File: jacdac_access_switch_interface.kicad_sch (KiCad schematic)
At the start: 43 parts

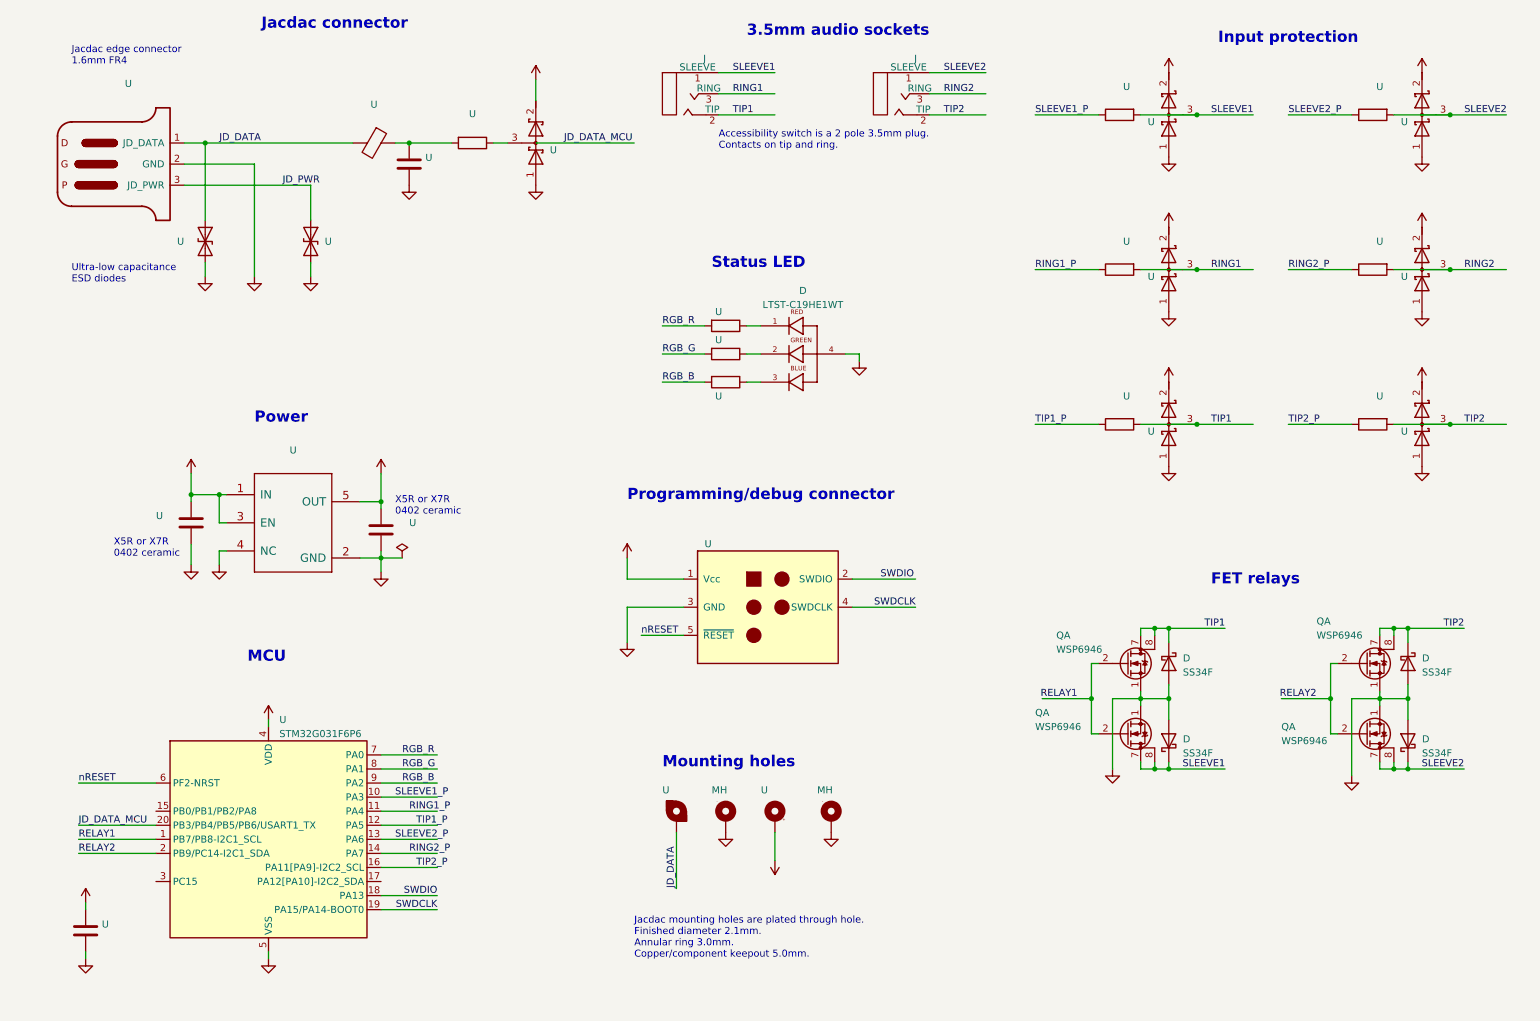
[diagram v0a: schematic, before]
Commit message: Changed MCU to STM32G030F6P6, updated input protection resistor to 10K, updated audio symbol
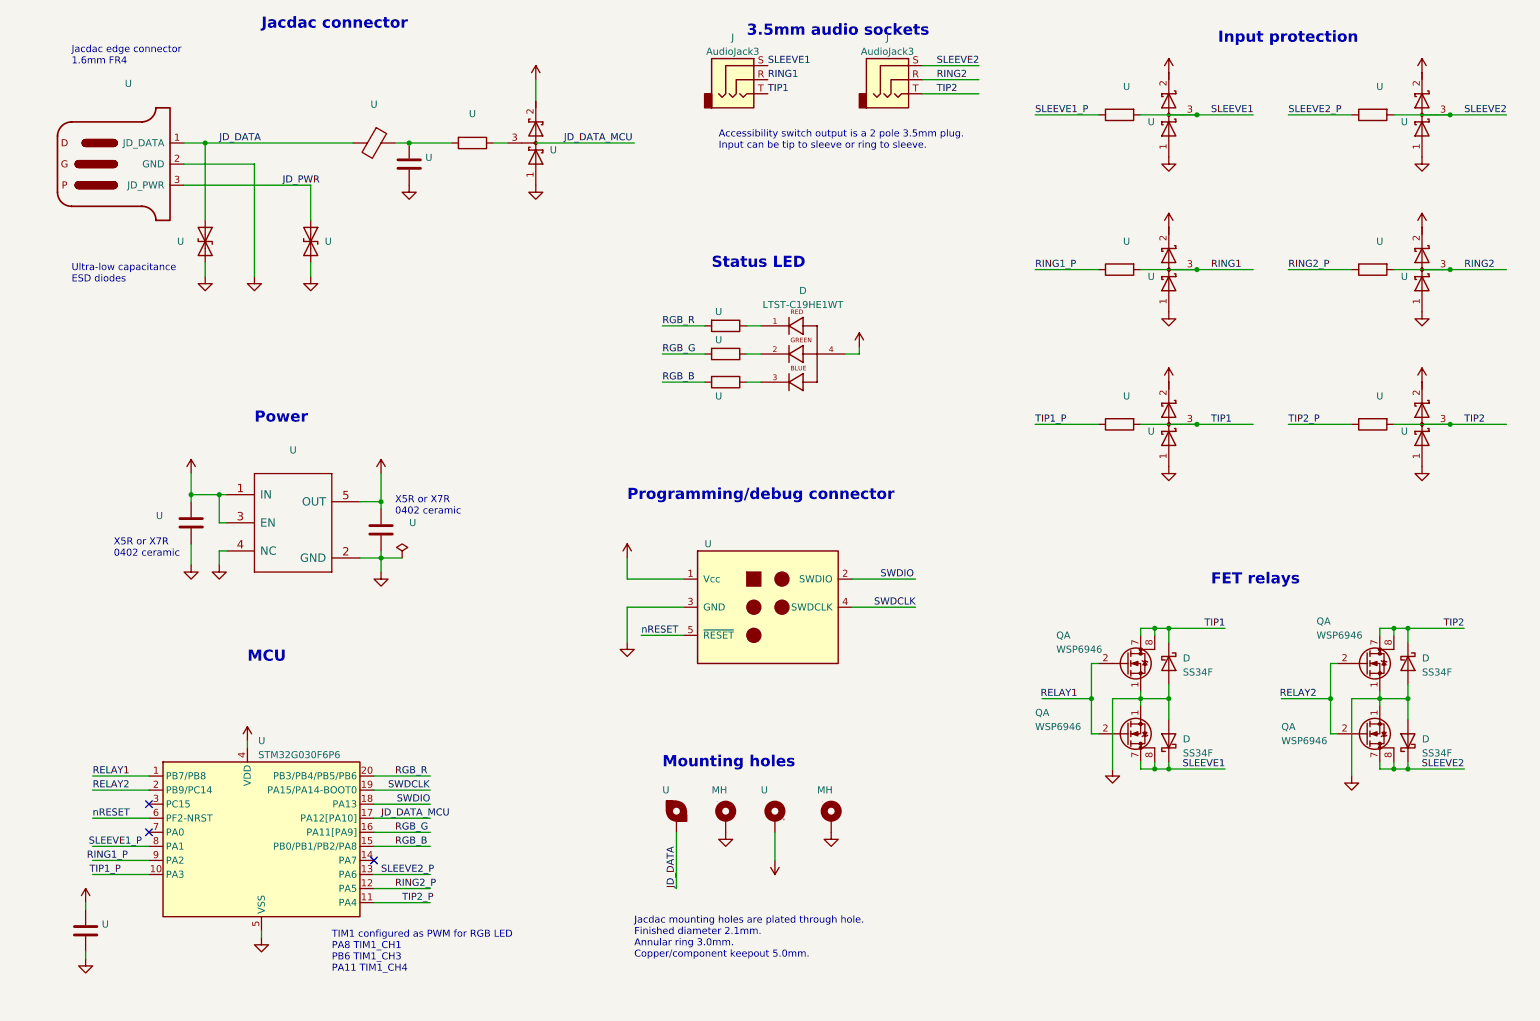
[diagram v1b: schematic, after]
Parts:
- removed J (x2): jack_3.5_pj313d, jacdac_access_switch_interface:jack_3.5_pj313d_smt, symbol jacdac_access_switch_interface:jack_3.5_pj313d
- removed U: STM32G031F6P6, Package_SO:TSSOP-20_4.4x6.5mm_P0.65mm, symbol jacdac_access_switch_interface:STM32G031F6P6
- added J (x2): AudioJack3, symbol jacdac_access_switch_interface:AudioJack3
- added U: STM32G030F6P6, jacdac_access_switch_interface:TSSOP-20_4.4x6.5mm_P0.65mm, symbol jacdac_access_switch_interface:STM32G030F6P6
- U: LCSC C138065 -> C60490
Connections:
- net +3V3: now also D.4, U.4 (VDD)
- net GND: now also U.5 (VSS); no longer D.4
- net JD_DATA_MCU: now also U.17 (PA12[PA10])
- net RELAY1: now also U.1 (PB7/PB8)
- net RELAY2: now also U.2 (PB9/PC14)
- net RGB_B: now also U.15 (PB0/PB1/PB2/PA8)
- net RGB_G: now also U.16 (PA11[PA9])
- net RGB_R: now also U.20 (PB3/PB4/PB5/PB6)
- net RING1: now also J.R
- net RING1_P: now also U.9 (PA2)
- net RING2: now also J.R
- net RING2_P: now also U.12 (PA5)
- net SLEEVE1: now also J.S
- net SLEEVE1_P: now also U.8 (PA1)
- net SLEEVE2: now also J.S
- net SLEEVE2_P: now also U.13 (PA6)
- net SWDCLK: now also U.19 (PA15/PA14-BOOT0)
- net SWDIO: now also U.18 (PA13)
- net TIP1: now also J.T
- net TIP1_P: now also U.10 (PA3)
- net TIP2: now also J.T
- net TIP2_P: now also U.11 (PA4)
- net nRESET: now also U.6 (PF2-NRST)
- no-connect marks 0 -> 3
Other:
- note added: "Accessibility switch output is a 2 pole 3.5mm plug. Input can be tip to sleeve or ring to sleeve."
- note added: "TIM1 configured as PWM for RGB LED PA8 TIM1_CH1 PB6 TIM1_CH3 PA11 TIM1_CH4"
- note removed: "Accessibility switch is a 2 pole 3.5mm plug. Contacts on tip and ring."

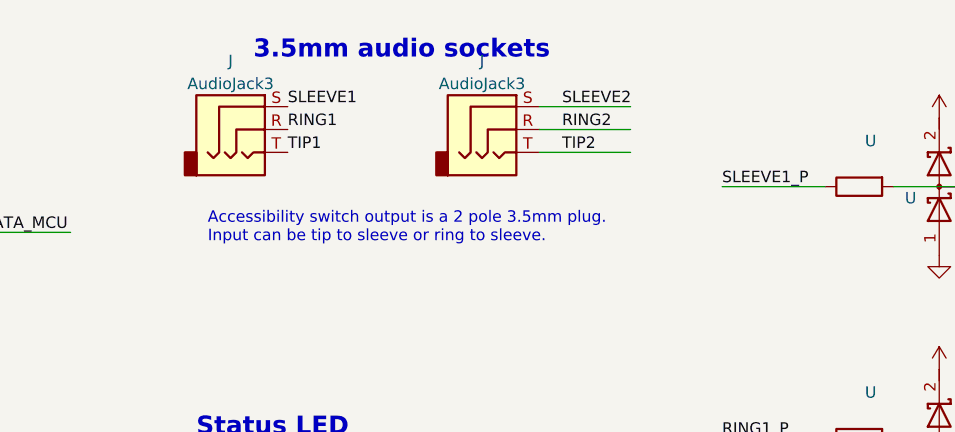
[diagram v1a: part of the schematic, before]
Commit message: Updated audio socket symbol
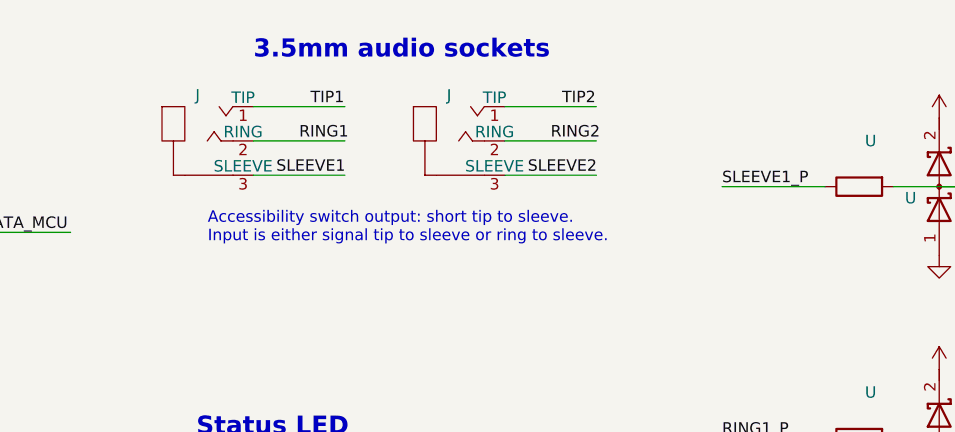
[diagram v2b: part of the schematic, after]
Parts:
- removed J (x2): AudioJack3, symbol jacdac_access_switch_interface:AudioJack3
- added J (x2): 54-00036_audio_plug, jacdac_access_switch_interface:Tensility-54-00036-0, symbol jacdac_access_switch_interface:54-00036_audio_plug
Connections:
- net RING1: now also J.2 (RING)
- net RING2: now also J.2 (RING)
- net SLEEVE1: now also J.3 (SLEEVE)
- net SLEEVE2: now also J.3 (SLEEVE)
- net TIP1: now also J.1 (TIP)
- net TIP2: now also J.1 (TIP)
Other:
- note added: "Accessibility switch output: short tip to sleeve. Input is either signal tip to sleeve or ring to sleeve."
- note removed: "Accessibility switch output is a 2 pole 3.5mm plug. Input can be tip to sleeve or ring to sleeve."
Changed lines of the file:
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@@
     (stroke (width 0) (type default))
   )
-  (wire (pts (xy 173.99 26.67) (xy 184.15 26.67))
+  (wire (pts (xy 170.18 34.29) (xy 180.34 34.29))
     (stroke (width 0) (type default))
   )
@@
     (stroke (width 0) (type default))
   )
+  (wire (pts (xy 142.24 34.29) (xy 152.4 34.29))
+    (stroke (width 0) (type default))
+  )
   (wire (pts (xy 76.2 105.41) (xy 76.2 106.68))
     (stroke (width 0) (type default))
@@
     (stroke (width 0) (type default))
   )
-  (wire (pts (xy 173.99 29.21) (xy 184.15 29.21))
-    (stroke (width 0) (type default))
-  )
-  (wire (pts (xy 173.99 31.75) (xy 184.15 31.75))
+  (wire (pts (xy 170.18 30.48) (xy 180.34 30.48))
+    (stroke (width 0) (type default))
+  )
+  (wire (pts (xy 170.18 26.67) (xy 180.34 26.67))
     (stroke (width 0) (type default))
   )
@@
     (stroke (width 0) (type default))
   )
+  (wire (pts (xy 142.24 26.67) (xy 152.4 26.67))
+    (stroke (width 0) (type default))
+  )
   (wire (pts (xy 256.54 153.67) (xy 259.08 153.67))
     (stroke (width 0) (type default))
@@
   )
   (wire (pts (xy 259.08 35.56) (xy 269.24 35.56))
+    (stroke (width 0) (type default))
+  )
+  (wire (pts (xy 142.24 30.48) (xy 152.4 30.48))
     (stroke (width 0) (type default))
   )
@@
     (effects (font (size 2.0066 2.0066) (thickness 0.4013) bold) (justify left bottom))
   )
-  (text "Accessibility switch output is a 2 pole 3.5mm plug. \nInput can be tip to sleeve or ring to sleeve."
+  (text "Accessibility switch output: short tip to sleeve.\nInput is either signal tip to sleeve or ring to sleeve."
     (at 137.16 41.91 0)
     (effects (font (size 1.27 1.27)) (justify left bottom))
@@
     (effects (font (size 1.27 1.27)) (justify left bottom))
   )
+  (label "RING1" (at 147.32 30.48 0) (fields_autoplaced)
+    (effects (font (size 1.27 1.27)) (justify left bottom))
+  )
   (label "RELAY1" (at 24.13 154.94 0) (fields_autoplaced)
     (effects (font (size 1.27 1.27)) (justify left bottom))
   )
-  (label "TIP2" (at 176.53 31.75 0) (fields_autoplaced)
+  (label "TIP2" (at 176.53 26.67 0) (fields_autoplaced)
     (effects (font (size 1.27 1.27)) (justify left bottom))
   )
@@
     (effects (font (size 1.27 1.27)) (justify right bottom))
   )
-  (label "TIP1" (at 146.05 31.75 0) (fields_autoplaced)
-    (effects (font (size 1.27 1.27)) (justify left bottom))
-  )
-  (label "RING2" (at 176.53 29.21 0) (fields_autoplaced)
+  (label "RING2" (at 175.26 30.48 0) (fields_autoplaced)
     (effects (font (size 1.27 1.27)) (justify left bottom))
   )
@@
     (effects (font (size 1.27 1.27)) (justify right bottom))
   )
+  (label "TIP1" (at 148.59 26.67 0) (fields_autoplaced)
+    (effects (font (size 1.27 1.27)) (justify left bottom))
+  )
   (label "SLEEVE2" (at 271.78 35.56 0) (fields_autoplaced)
     (effects (font (size 1.27 1.27)) (justify left bottom))
   )
-  (label "RING1" (at 146.05 29.21 0) (fields_autoplaced)
-    (effects (font (size 1.27 1.27)) (justify left bottom))
-  )
   (label "JD_DATA_MCU" (at 109.22 40.64 0) (fields_autoplaced)
     (effects (font (size 1.27 1.27)) (justify left bottom))
@@
   )
   (label "JD_DATA" (at 46.99 40.64 0) (fields_autoplaced)
-    (effects (font (size 1.27 1.27)) (justify left bottom))
-  )
-  (label "SLEEVE1" (at 146.05 26.67 0) (fields_autoplaced)
     (effects (font (size 1.27 1.27)) (justify left bottom))
   )
@@
     (effects (font (size 1.27 1.27)) (justify right bottom))
   )
+  (label "SLEEVE1" (at 144.78 34.29 0) (fields_autoplaced)
+    (effects (font (size 1.27 1.27)) (justify left bottom))
+  )
   (label "JD_PWR" (at 58.42 48.26 0) (fields_autoplaced)
     (effects (font (size 1.27 1.27)) (justify left bottom))
@@
     (effects (font (size 1.27 1.27)) (justify left bottom))
   )
-  (label "SLEEVE2" (at 176.53 26.67 0) (fields_autoplaced)
+  (label "SLEEVE2" (at 172.72 34.29 0) (fields_autoplaced)
     (effects (font (size 1.27 1.27)) (justify left bottom))
   )
@@
     (pin "1")
     (pin "2")
-  )
-  (symbol (lib_id "jacdac_access_switch_interface:AudioJack3") (at 140.97 29.21 0) (unit 1)
-    (in_bom yes) (on_board yes)
-    (default_instance (reference "J") (unit 1) (value "AudioJack3") (footprint ""))
-    (property "Reference" "J" (id 0) (at 139.7 21.59 0)
-      (effects (font (size 1.27 1.27)))
-    )
-    (property "Value" "AudioJack3" (id 1) (at 139.7 24.13 0)
-      (effects (font (size 1.27 1.27)))
-    )
-    (property "Footprint" "" (id 2) (at 140.97 29.21 0)
-      (effects (font (size 1.27 1.27)) hide)
-    )
-    (property "Datasheet" "~" (id 3) (at 140.97 29.21 0)
-      (effects (font (size 1.27 1.27)) hide)
-    )
-    (pin "R")
-    (pin "S")
-    (pin "T")
-  )
-  (symbol (lib_id "jacdac_access_switch_interface:AudioJack3") (at 168.91 29.21 0) (unit 1)
-    (in_bom yes) (on_board yes)
-    (default_instance (reference "J") (unit 1) (value "AudioJack3") (footprint ""))
-    (property "Reference" "J" (id 0) (at 167.64 21.59 0)
-      (effects (font (size 1.27 1.27)))
-    )
-    (property "Value" "AudioJack3" (id 1) (at 167.64 24.13 0)
-      (effects (font (size 1.27 1.27)))
-    )
-    (property "Footprint" "" (id 2) (at 168.91 29.21 0)
-      (effects (font (size 1.27 1.27)) hide)
-    )
-    (property "Datasheet" "~" (id 3) (at 168.91 29.21 0)
-      (effects (font (size 1.27 1.27)) hide)
-    )
-    (pin "R")
-    (pin "S")
-    (pin "T")
   )
   (symbol (lib_id "power:GND") (at 264.16 43.18 0) (mirror y) (unit 1)
@@
     (pin "1")
   )
+  (symbol (lib_id "jacdac_access_switch_interface:54-00036_audio_plug") (at 139.7 30.48 0) (unit 1)
+    (in_bom yes) (on_board yes) (fields_autoplaced)
+    (default_instance (reference "J") (unit 1) (value "54-00036_audio_plug") (footprint "jacdac_access_switch_interface:Tensility-54-00036-0"))
+    (property "Reference" "J" (id 0) (at 136.0424 25.4 0)
+      (effects (font (size 1.27 1.27)))
+    )
+    (property "Value" "54-00036_audio_plug" (id 1) (at 130.81 38.1 0)
+      (effects (font (size 1.27 1.27)) (justify left) hide)
+    )
+    (property "Footprint" "jacdac_access_switch_interface:Tensility-54-00036-0" (id 2) (at 130.81 20.32 0)
+      (effects (font (size 1.27 1.27)) (justify left) hide)
+    )
+    (property "Datasheet" "http://www.tensility.com/pdffiles/54-00036.pdf" (id 3) (at 130.81 17.78 0)
+      (effects (font (size 1.27 1.27)) (justify left) hide)
+    )
+    (property "digikey description" "CONN PLUG STEREO 3.5MM RA 3COND" (id 4) (at 130.81 15.24 0)
+      (effects (font (size 1.27 1.27)) (justify left) hide)
+    )
+    (property "digikey part number" "839-1240-ND" (id 5) (at 130.81 12.7 0)
+      (effects (font (size 1.27 1.27)) (justify left) hide)
+    )
+    (property "package" "JACK_PTH" (id 6) (at 130.81 10.16 0)
+      (effects (font (size 1.27 1.27)) (justify left) hide)
+    )
+    (pin "1")
+    (pin "2")
+    (pin "3")
+  )
   (symbol (lib_id "Device:D_Schottky_Dual_Series_AKC") (at 218.44 91.44 90) (unit 1)
     (in_bom yes) (on_board yes)
@@
     (pin "1")
   )
+  (symbol (lib_id "jacdac_access_switch_interface:54-00036_audio_plug") (at 167.64 30.48 0) (unit 1)
+    (in_bom yes) (on_board yes) (fields_autoplaced)
+    (default_instance (reference "J") (unit 1) (value "54-00036_audio_plug") (footprint "jacdac_access_switch_interface:Tensility-54-00036-0"))
+    (property "Reference" "J" (id 0) (at 163.9824 25.4 0)
+      (effects (font (size 1.27 1.27)))
+    )
+    (property "Value" "54-00036_audio_plug" (id 1) (at 158.75 38.1 0)
+      (effects (font (size 1.27 1.27)) (justify left) hide)
+    )
+    (property "Footprint" "jacdac_access_switch_interface:Tensility-54-00036-0" (id 2) (at 158.75 20.32 0)
+      (effects (font (size 1.27 1.27)) (justify left) hide)
+    )
+    (property "Datasheet" "http://www.tensility.com/pdffiles/54-00036.pdf" (id 3) (at 158.75 17.78 0)
+      (effects (font (size 1.27 1.27)) (justify left) hide)
+    )
+    (property "digikey description" "CONN PLUG STEREO 3.5MM RA 3COND" (id 4) (at 158.75 15.24 0)
+      (effects (font (size 1.27 1.27)) (justify left) hide)
+    )
+    (property "digikey part number" "839-1240-ND" (id 5) (at 158.75 12.7 0)
+      (effects (font (size 1.27 1.27)) (justify left) hide)
+    )
+    (property "package" "JACK_PTH" (id 6) (at 158.75 10.16 0)
+      (effects (font (size 1.27 1.27)) (justify left) hide)
+    )
+    (pin "1")
+    (pin "2")
+    (pin "3")
+  )
   (symbol (lib_id "jacdac_access_switch_interface:SS34F") (at 261.62 148.59 90) (unit 1)
     (in_bom yes) (on_board yes) (fields_autoplaced)
@@
       (reference "J2") (unit 1) (value "Conn_HackConnect") (footprint "Jacdac:HackConnect_P1.27mm")
     )
-    (path "/0ea409df-7627-4a38-aea6-9a9b261767d5"
-      (reference "J5") (unit 1) (value "AudioJack3") (footprint "")
-    )
-    (path "/127a46cb-e96e-4de9-979b-f8d631e6b382"
-      (reference "J6") (unit 1) (value "AudioJack3") (footprint "")
+    (path "/9a2a0c50-9d61-467f-a7f1-d5a5b368c077"
+      (reference "J3") (unit 1) (value "54-00036_audio_plug") (footprint "jacdac_access_switch_interface:Tensility-54-00036-0")
+    )
+    (path "/c97270aa-f798-4af1-8c2a-c0745fb1b88e"
+      (reference "J4") (unit 1) (value "54-00036_audio_plug") (footprint "jacdac_access_switch_interface:Tensility-54-00036-0")
     )
     (path "/00000000-0000-0000-0000-000060fae86c"
